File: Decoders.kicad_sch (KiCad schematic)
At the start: 37 parts, among them U10 CD74HC238PWR, U11 CD74HC238PWR, U12 CD74HC238PWR, U13 CD74HC238PWR, U14 ULN2003ADR, U15 ULN2003ADR, U16 CD74HC238PWR, U17 CD74HC238PWR, U18 CD74HC238PWR, U19 CD74HC238PWR, U20 ULN2003ADR, U21 ULN2003ADR, U22 CD74HC238PWR, U23 CD74HC238PWR, U24 ULN2003ADR, U25 CD74HC238PWR, U26 CD74HC238PWR, U27 CD74HC238PWR, U28 CD74HC238PWR, U8 ULN2003ADR, U9 ULN2003ADR

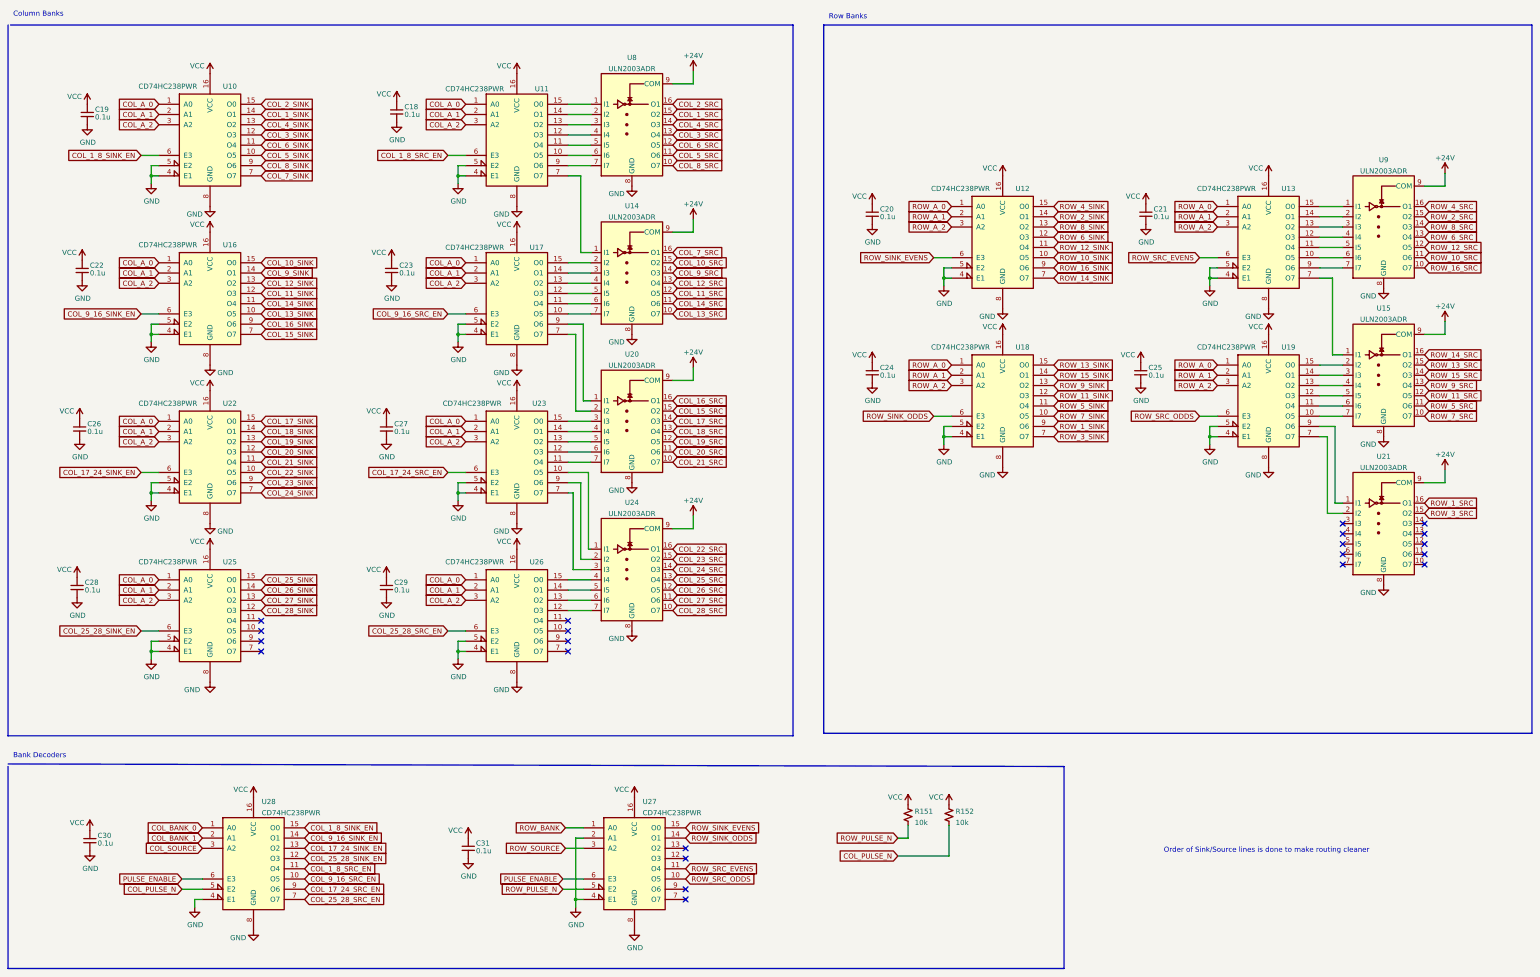
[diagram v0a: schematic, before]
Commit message: Add subrevision, reference submodule objects
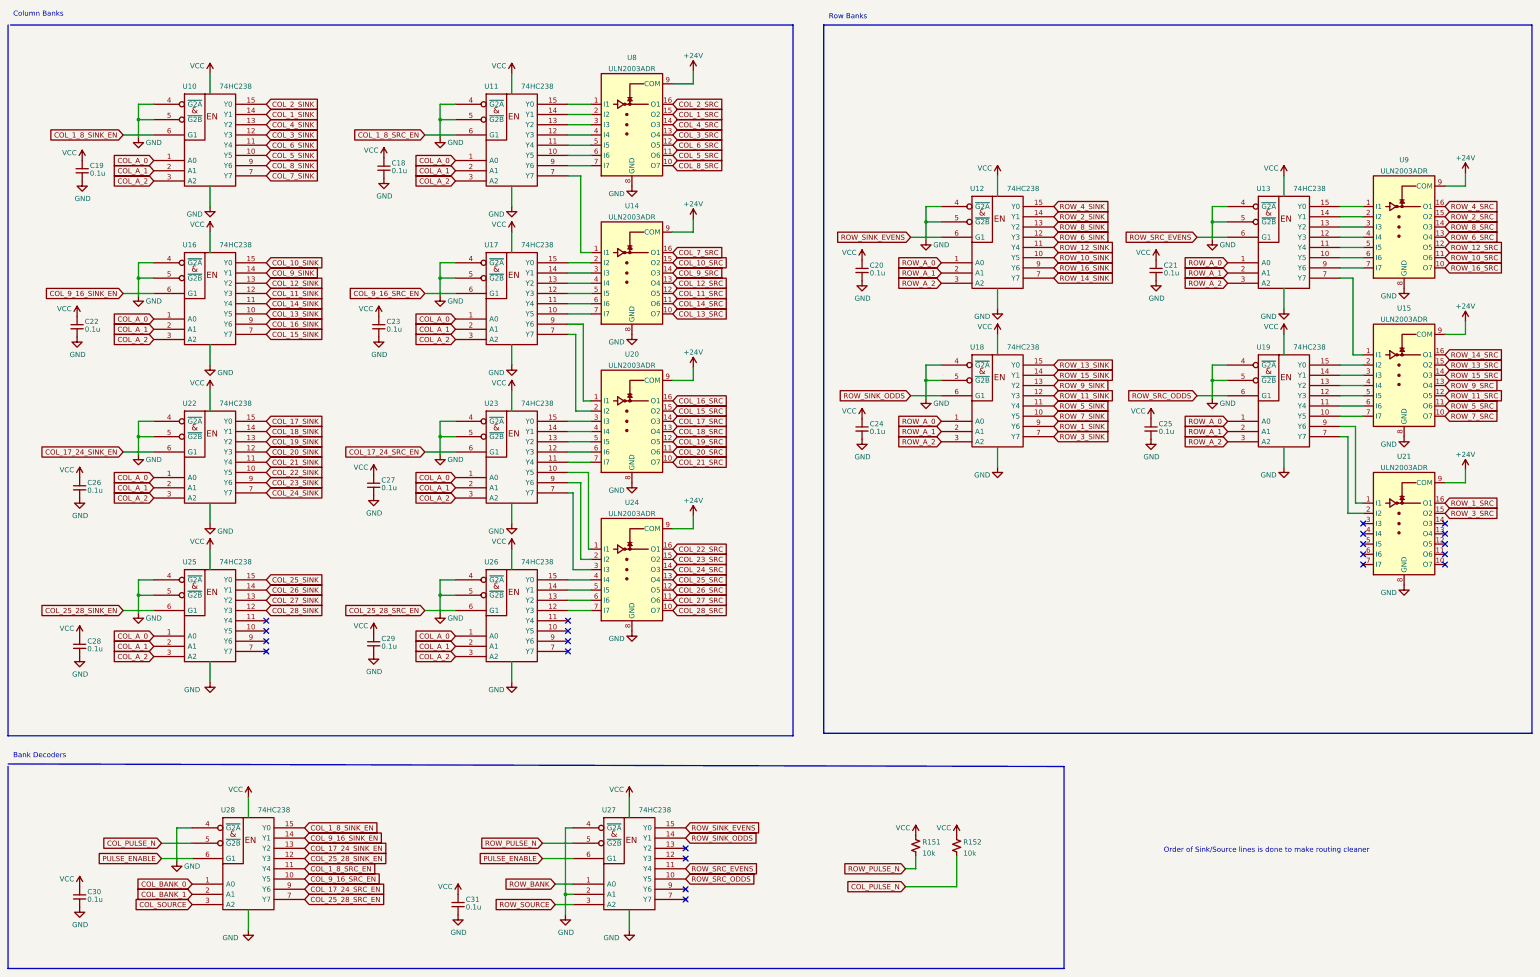
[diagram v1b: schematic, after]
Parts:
- removed U10, U11, U12, U13, U16, U17, U18, U19, U22, U23, U25, U26, U27, U28: CD74HC238PWR, Package_SO:TSSOP-16_4.4x5mm_P0.65mm, symbol Common:MC74HC238
- added U10, U11, U12, U13, U16, U17, U18, U19, U22, U23, U25, U26, U27, U28: 74HC238, Package_SO:TSSOP-16_4.4x5mm_P0.65mm, symbol 74xx_IEEE:74HC238
- U14, U15, U20, U21, U24, U8, U9: Digikey (none) -> 595-ULN2003ADR
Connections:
- net COL_10_SINK: now also U16.15 (Y0)
- net COL_11_SINK: now also U16.12 (Y3)
- net COL_12_SINK: now also U16.13 (Y2)
- net COL_13_SINK: now also U16.10 (Y5)
- net COL_14_SINK: now also U16.11 (Y4)
- net COL_15_SINK: now also U16.7 (Y7)
- net COL_16_SINK: now also U16.9 (Y6)
- net COL_17_24_SINK_EN: now also U22.6 (G1), U28.13 (Y2)
- net COL_17_24_SRC_EN: now also U23.6 (G1), U28.9 (Y6)
- net COL_17_SINK: now also U22.15 (Y0)
- net COL_18_SINK: now also U22.14 (Y1)
- net COL_19_SINK: now also U22.13 (Y2)
- net COL_1_8_SINK_EN: now also U10.6 (G1), U28.15 (Y0)
- net COL_1_8_SRC_EN: now also U11.6 (G1), U28.11 (Y4)
- net COL_1_SINK: now also U10.14 (Y1)
- net COL_20_SINK: now also U22.12 (Y3)
- net COL_21_SINK: now also U22.11 (Y4)
- net COL_22_SINK: now also U22.10 (Y5)
- net COL_23_SINK: now also U22.9 (Y6)
- net COL_24_SINK: now also U22.7 (Y7)
- net COL_25_28_SINK_EN: now also U25.6 (G1), U28.12 (Y3)
- net COL_25_28_SRC_EN: now also U26.6 (G1), U28.7 (Y7)
- net COL_25_SINK: now also U25.15 (Y0)
- net COL_26_SINK: now also U25.14 (Y1)
- net COL_27_SINK: now also U25.13 (Y2)
- net COL_28_SINK: now also U25.12 (Y3)
- net COL_2_SINK: now also U10.15 (Y0)
- net COL_3_SINK: now also U10.12 (Y3)
- net COL_4_SINK: now also U10.13 (Y2)
- net COL_5_SINK: now also U10.10 (Y5)
- net COL_6_SINK: now also U10.11 (Y4)
- net COL_7_SINK: now also U10.7 (Y7)
- net COL_8_SINK: now also U10.9 (Y6)
- net COL_9_16_SINK_EN: now also U16.6 (G1), U28.14 (Y1)
- net COL_9_16_SRC_EN: now also U17.6 (G1), U28.10 (Y5)
- net COL_9_SINK: now also U16.14 (Y1)
- net COL_A_0: now also U10.1 (A0), U11.1 (A0), U16.1 (A0), U17.1 (A0), U22.1 (A0), U23.1 (A0), U25.1 (A0), U26.1 (A0)
- net COL_A_1: now also U10.2 (A1), U11.2 (A1), U16.2 (A1), U17.2 (A1), U22.2 (A1), U23.2 (A1), U25.2 (A1), U26.2 (A1)
- net COL_A_2: now also U10.3 (A2), U11.3 (A2), U16.3 (A2), U17.3 (A2), U22.3 (A2), U23.3 (A2), U25.3 (A2), U26.3 (A2)
- net COL_BANK_0: now also U28.1 (A0)
- net COL_BANK_1: now also U28.2 (A1)
- net COL_PULSE_N: now also U28.5 (~{G2B})
- net COL_SOURCE: now also U28.3 (A2)
- net GND: now also U10.4 (~{G2A}), U10.5 (~{G2B}), U10.8 (GND), U11.4 (~{G2A}), U11.5 (~{G2B}), U11.8 (GND), U12.4 (~{G2A}), U12.5 (~{G2B}), U12.8 (GND), U13.4 (~{G2A}), U13.5 (~{G2B}), U13.8 (GND), U16.4 (~{G2A}), U16.5 (~{G2B}), U16.8 (GND), U17.4 (~{G2A}), U17.5 (~{G2B}), U17.8 (GND), U18.4 (~{G2A}), U18.5 (~{G2B}), U18.8 (GND), U19.4 (~{G2A}), U19.5 (~{G2B}), U19.8 (GND), U22.4 (~{G2A}), U22.5 (~{G2B}), U22.8 (GND), U23.4 (~{G2A}), U23.5 (~{G2B}), U23.8 (GND), U25.4 (~{G2A}), U25.5 (~{G2B}), U25.8 (GND), U26.4 (~{G2A}), U26.5 (~{G2B}), U26.8 (GND), U27.2 (A1), U27.4 (~{G2A}), U27.8 (GND), U28.4 (~{G2A}), U28.8 (GND)
- net PULSE_ENABLE: now also U27.6 (G1), U28.6 (G1)
- net ROW_10_SINK: now also U12.10 (Y5)
- net ROW_11_SINK: now also U18.12 (Y3)
- net ROW_12_SINK: now also U12.11 (Y4)
- net ROW_13_SINK: now also U18.15 (Y0)
- net ROW_14_SINK: now also U12.7 (Y7)
- net ROW_15_SINK: now also U18.14 (Y1)
- net ROW_16_SINK: now also U12.9 (Y6)
- net ROW_1_SINK: now also U18.9 (Y6)
- net ROW_2_SINK: now also U12.14 (Y1)
- net ROW_3_SINK: now also U18.7 (Y7)
- net ROW_4_SINK: now also U12.15 (Y0)
- net ROW_5_SINK: now also U18.11 (Y4)
- net ROW_6_SINK: now also U12.12 (Y3)
- net ROW_7_SINK: now also U18.10 (Y5)
- net ROW_8_SINK: now also U12.13 (Y2)
- net ROW_9_SINK: now also U18.13 (Y2)
- net ROW_A_0: now also U12.1 (A0), U13.1 (A0), U18.1 (A0), U19.1 (A0)
- net ROW_A_1: now also U12.2 (A1), U13.2 (A1), U18.2 (A1), U19.2 (A1)
- net ROW_A_2: now also U12.3 (A2), U13.3 (A2), U18.3 (A2), U19.3 (A2)
- net ROW_BANK: now also U27.1 (A0)
- net ROW_PULSE_N: now also U27.5 (~{G2B})
- net ROW_SINK_EVENS: now also U12.6 (G1), U27.15 (Y0)
- net ROW_SINK_ODDS: now also U18.6 (G1), U27.14 (Y1)
- net ROW_SOURCE: now also U27.3 (A2)
- net ROW_SRC_EVENS: now also U13.6 (G1), U27.11 (Y4)
- net ROW_SRC_ODDS: now also U19.6 (G1), U27.10 (Y5)
- net VCC: now also U10.16 (VCC), U11.16 (VCC), U12.16 (VCC), U13.16 (VCC), U16.16 (VCC), U17.16 (VCC), U18.16 (VCC), U19.16 (VCC), U22.16 (VCC), U23.16 (VCC), U25.16 (VCC), U26.16 (VCC), U27.16 (VCC), U28.16 (VCC)
- net at U15.7 (I7): now also U19.10 (Y5)
- net at U15.6 (I6): now also U19.11 (Y4)
- net at U15.5 (I5): now also U19.12 (Y3)
- net at U15.4 (I4): now also U19.13 (Y2)
- net at U15.3 (I3): now also U19.14 (Y1)
- net at U15.2 (I2): now also U19.15 (Y0)
- net at U21.2 (I2): now also U19.7 (Y7)
- net at U21.1 (I1): now also U19.9 (Y6)
- net at U15.1 (I1): now also U13.7 (Y7)
- net at U24.1 (I1): now also U23.10 (Y5)
- net at U20.7 (I7): now also U23.11 (Y4)
- net at U20.6 (I6): now also U23.12 (Y3)
- net at U20.5 (I5): now also U23.13 (Y2)
- net at U20.4 (I4): now also U23.14 (Y1)
- net at U20.3 (I3): now also U23.15 (Y0)
- net at U24.3 (I3): now also U23.7 (Y7)
- net at U24.2 (I2): now also U23.9 (Y6)
- net at U14.7 (I7): now also U17.10 (Y5)
- net at U14.6 (I6): now also U17.11 (Y4)
- net at U14.5 (I5): now also U17.12 (Y3)
- net at U14.4 (I4): now also U17.13 (Y2)
- net at U14.3 (I3): now also U17.14 (Y1)
- net at U14.2 (I2): now also U17.15 (Y0)
- net at U20.2 (I2): now also U17.7 (Y7)
- net at U20.1 (I1): now also U17.9 (Y6)
- net at U8.6 (I6): now also U11.10 (Y5)
- net at U8.5 (I5): now also U11.11 (Y4)
- net at U8.4 (I4): now also U11.12 (Y3)
- net at U8.3 (I3): now also U11.13 (Y2)
- net at U8.2 (I2): now also U11.14 (Y1)
- net at U8.1 (I1): now also U11.15 (Y0)
- net at U14.1 (I1): now also U11.7 (Y7)
- net at U8.7 (I7): now also U11.9 (Y6)
- net at U24.4 (I4): now also U26.15 (Y0)
- net at U24.5 (I5): now also U26.14 (Y1)
- net at U24.6 (I6): now also U26.13 (Y2)
- net at U24.7 (I7): now also U26.12 (Y3)
- net at U9.6 (I6): now also U13.10 (Y5)
- net at U9.5 (I5): now also U13.11 (Y4)
- net at U9.4 (I4): now also U13.12 (Y3)
- net at U9.3 (I3): now also U13.13 (Y2)
- net at U9.2 (I2): now also U13.14 (Y1)
- net at U9.1 (I1): now also U13.15 (Y0)
- net at U9.7 (I7): now also U13.9 (Y6)
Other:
- moved on the sheet: C18, C19, C20, C21, C22, C23, C24, C25, C26, C27, C28, C29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

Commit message: Initial draft of Revision D
- Remove I2C Bus, and replace with PWM Input
- Remove temp sensors due to no I2C bus
- Add 5V aux output from 24V, supports LM7805 (w/ Heatsink) and VX7805
- Larger components for high current nets
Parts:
- U10, U11, U12, U13, U16, U17, U18, U19, U22, U23, U25, U26, U27, U28: Digikey (none) -> 296-33050-5-ND; LCSC (none) -> C403724
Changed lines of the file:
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@@
   (title_block
     (title "Luminator MAX3000 Custom Driver Board")
-    (date "2022-08-16")
-    (rev "C.2")
+    (date "2022-08-30")
+    (rev "D")
     (comment 2 "To SET, current flows from ROW_SET to COL ")
     (comment 3 "To RESET, current flows from COL to ROW_RESET")
@@
       (effects (font (size 1.27 1.27)) hide)
     )
+    (property "Digikey" "296-33050-5-ND" (id 4) (at 342.9 116.84 0)
+      (effects (font (size 1.27 1.27)) hide)
+    )
+    (property "LCSC" "C403724" (id 5) (at 342.9 116.84 0)
+      (effects (font (size 1.27 1.27)) hide)
+    )
     (pin "16")
     (pin "1")
@@
       (effects (font (size 1.27 1.27)) hide)
     )
+    (property "Digikey" "296-33050-5-ND" (id 4) (at 151.13 170.18 0)
+      (effects (font (size 1.27 1.27)) hide)
+    )
+    (property "LCSC" "C403724" (id 5) (at 151.13 170.18 0)
+      (effects (font (size 1.27 1.27)) hide)
+    )
     (pin "16")
     (pin "1")
@@
       (effects (font (size 1.27 1.27)) hide)
     )
+    (property "Digikey" "296-33050-5-ND" (id 4) (at 76.2 130.81 0)
+      (effects (font (size 1.27 1.27)) hide)
+    )
+    (property "LCSC" "C403724" (id 5) (at 76.2 130.81 0)
+      (effects (font (size 1.27 1.27)) hide)
+    )
     (pin "16")
     (pin "1")
@@
       (effects (font (size 1.27 1.27)) hide)
     )
+    (property "Digikey" "296-33050-5-ND" (id 4) (at 76.2 91.44 0)
+      (effects (font (size 1.27 1.27)) hide)
+    )
+    (property "LCSC" "C403724" (id 5) (at 76.2 91.44 0)
+      (effects (font (size 1.27 1.27)) hide)
+    )
     (pin "16")
     (pin "1")
@@
       (effects (font (size 1.27 1.27)) hide)
     )
+    (property "Digikey" "296-33050-5-ND" (id 4) (at 151.13 130.81 0)
+      (effects (font (size 1.27 1.27)) hide)
+    )
+    (property "LCSC" "C403724" (id 5) (at 151.13 130.81 0)
+      (effects (font (size 1.27 1.27)) hide)
+    )
     (pin "16")
     (pin "1")
@@
       (effects (font (size 1.27 1.27)) hide)
     )
+    (property "Digikey" "296-33050-5-ND" (id 4) (at 342.9 77.47 0)
+      (effects (font (size 1.27 1.27)) hide)
+    )
+    (property "LCSC" "C403724" (id 5) (at 342.9 77.47 0)
+      (effects (font (size 1.27 1.27)) hide)
+    )
     (pin "16")
     (pin "1")
@@
       (effects (font (size 1.27 1.27)) hide)
     )
+    (property "Digikey" "296-33050-5-ND" (id 4) (at 151.13 52.07 0)
+      (effects (font (size 1.27 1.27)) hide)
+    )
+    (property "LCSC" "C403724" (id 5) (at 151.13 52.07 0)
+      (effects (font (size 1.27 1.27)) hide)
+    )
     (pin "16")
     (pin "1")
@@
       (effects (font (size 1.27 1.27)) hide)
     )
+    (property "Digikey" "296-33050-5-ND" (id 4) (at 85.725 231.775 0)
+      (effects (font (size 1.27 1.27)) hide)
+    )
+    (property "LCSC" "C403724" (id 5) (at 85.725 231.775 0)
+      (effects (font (size 1.27 1.27)) hide)
+    )
     (pin "16")
     (pin "1")
@@
       (effects (font (size 1.27 1.27)) hide)
     )
+    (property "Digikey" "296-33050-5-ND" (id 4) (at 76.2 52.07 0)
+      (effects (font (size 1.27 1.27)) hide)
+    )
+    (property "LCSC" "C403724" (id 5) (at 76.2 52.07 0)
+      (effects (font (size 1.27 1.27)) hide)
+    )
     (pin "16")
     (pin "1")
@@
       (effects (font (size 1.27 1.27)) hide)
     )
+    (property "Digikey" "296-33050-5-ND" (id 4) (at 151.13 91.44 0)
+      (effects (font (size 1.27 1.27)) hide)
+    )
+    (property "LCSC" "C403724" (id 5) (at 151.13 91.44 0)
+      (effects (font (size 1.27 1.27)) hide)
+    )
     (pin "16")
     (pin "1")
@@
       (effects (font (size 1.27 1.27)) hide)
     )
+    (property "Digikey" "296-33050-5-ND" (id 4) (at 76.2 170.18 0)
+      (effects (font (size 1.27 1.27)) hide)
+    )
+    (property "LCSC" "C403724" (id 5) (at 76.2 170.18 0)
+      (effects (font (size 1.27 1.27)) hide)
+    )
     (pin "16")
     (pin "1")
@@
       (effects (font (size 1.27 1.27)) hide)
     )
+    (property "Digikey" "296-33050-5-ND" (id 4) (at 180.34 231.775 0)
+      (effects (font (size 1.27 1.27)) hide)
+    )
+    (property "LCSC" "C403724" (id 5) (at 180.34 231.775 0)
+      (effects (font (size 1.27 1.27)) hide)
+    )
     (pin "16")
     (pin "1")
@@
       (effects (font (size 1.27 1.27)) hide)
     )
+    (property "Digikey" "296-33050-5-ND" (id 4) (at 271.78 77.47 0)
+      (effects (font (size 1.27 1.27)) hide)
+    )
+    (property "LCSC" "C403724" (id 5) (at 271.78 77.47 0)
+      (effects (font (size 1.27 1.27)) hide)
+    )
     (pin "16")
     (pin "1")
@@
       (effects (font (size 1.27 1.27)) hide)
     )
+    (property "Digikey" "296-33050-5-ND" (id 4) (at 271.78 116.84 0)
+      (effects (font (size 1.27 1.27)) hide)
+    )
+    (property "LCSC" "C403724" (id 5) (at 271.78 116.84 0)
+      (effects (font (size 1.27 1.27)) hide)
+    )

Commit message: Replace LCSC parts with ones in stock
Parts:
- U10, U11, U12, U13, U16, U17, U18, U19, U22, U23, U25, U26, U27, U28: LCSC C403724 -> C60434
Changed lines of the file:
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@@
       (effects (font (size 1.27 1.27)) hide)
     )
-    (property "LCSC" "C403724" (id 5) (at 342.9 116.84 0)
+    (property "LCSC" "C60434" (id 5) (at 342.9 116.84 0)
       (effects (font (size 1.27 1.27)) hide)
     )
@@
       (effects (font (size 1.27 1.27)) hide)
     )
-    (property "LCSC" "C403724" (id 5) (at 151.13 170.18 0)
+    (property "LCSC" "C60434" (id 5) (at 151.13 170.18 0)
       (effects (font (size 1.27 1.27)) hide)
     )
@@
       (effects (font (size 1.27 1.27)) hide)
     )
-    (property "LCSC" "C403724" (id 5) (at 76.2 130.81 0)
+    (property "LCSC" "C60434" (id 5) (at 76.2 130.81 0)
       (effects (font (size 1.27 1.27)) hide)
     )
@@
       (effects (font (size 1.27 1.27)) hide)
     )
-    (property "LCSC" "C403724" (id 5) (at 76.2 91.44 0)
+    (property "LCSC" "C60434" (id 5) (at 76.2 91.44 0)
       (effects (font (size 1.27 1.27)) hide)
     )
@@
       (effects (font (size 1.27 1.27)) hide)
     )
-    (property "LCSC" "C403724" (id 5) (at 151.13 130.81 0)
+    (property "LCSC" "C60434" (id 5) (at 151.13 130.81 0)
       (effects (font (size 1.27 1.27)) hide)
     )
@@
       (effects (font (size 1.27 1.27)) hide)
     )
-    (property "LCSC" "C403724" (id 5) (at 342.9 77.47 0)
+    (property "LCSC" "C60434" (id 5) (at 342.9 77.47 0)
       (effects (font (size 1.27 1.27)) hide)
     )
@@
       (effects (font (size 1.27 1.27)) hide)
     )
-    (property "LCSC" "C403724" (id 5) (at 151.13 52.07 0)
+    (property "LCSC" "C60434" (id 5) (at 151.13 52.07 0)
       (effects (font (size 1.27 1.27)) hide)
     )
@@
       (effects (font (size 1.27 1.27)) hide)
     )
-    (property "LCSC" "C403724" (id 5) (at 85.725 231.775 0)
+    (property "LCSC" "C60434" (id 5) (at 85.725 231.775 0)
       (effects (font (size 1.27 1.27)) hide)
     )
@@
       (effects (font (size 1.27 1.27)) hide)
     )
-    (property "LCSC" "C403724" (id 5) (at 76.2 52.07 0)
+    (property "LCSC" "C60434" (id 5) (at 76.2 52.07 0)
       (effects (font (size 1.27 1.27)) hide)
     )
@@
       (effects (font (size 1.27 1.27)) hide)
     )
-    (property "LCSC" "C403724" (id 5) (at 151.13 91.44 0)
+    (property "LCSC" "C60434" (id 5) (at 151.13 91.44 0)
       (effects (font (size 1.27 1.27)) hide)
     )
@@
       (effects (font (size 1.27 1.27)) hide)
     )
-    (property "LCSC" "C403724" (id 5) (at 76.2 170.18 0)
+    (property "LCSC" "C60434" (id 5) (at 76.2 170.18 0)
       (effects (font (size 1.27 1.27)) hide)
     )
@@
       (effects (font (size 1.27 1.27)) hide)
     )
-    (property "LCSC" "C403724" (id 5) (at 180.34 231.775 0)
+    (property "LCSC" "C60434" (id 5) (at 180.34 231.775 0)
       (effects (font (size 1.27 1.27)) hide)
     )
@@
       (effects (font (size 1.27 1.27)) hide)
     )
-    (property "LCSC" "C403724" (id 5) (at 271.78 77.47 0)
+    (property "LCSC" "C60434" (id 5) (at 271.78 77.47 0)
       (effects (font (size 1.27 1.27)) hide)
     )
@@
       (effects (font (size 1.27 1.27)) hide)
     )
-    (property "LCSC" "C403724" (id 5) (at 271.78 116.84 0)
-      (effects (font (size 1.27 1.27)) hide)
-    )
+    (property "LCSC" "C60434" (id 5) (at 271.78 116.84 0)
+      (effects (font (size 1.27 1.27)) hide)
+    )
